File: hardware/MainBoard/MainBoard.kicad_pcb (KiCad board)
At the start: 4 copper layers, 28.6 x 59.4 mm, 54 parts, among them J1 Conn_02x16_Top_Bottom, J2 Conn_02x16_Top_Bottom, J3 USB_C_Receptacle_USB2.0_16P, J4 En_A, J5 En_B, J6 Micro_SD_Card_Det2, J7 Conn_02x16_Top_Bottom, Q1 MMBT2222A, U1 ESP32-S3-WROOM-1, U2 AMS1117-3.3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

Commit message: main board stuff
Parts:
- J1: moved to F.Cu
- J2: moved to B.Cu
- moved G*** 38.1 mm to (35.6, 70.9)
- moved J1 25.0 mm to (58.8, 91.8), turned to -90 degrees
- moved BOOT1 15.4 mm to (50.5, 64.7)
- moved R12 15.4 mm to (50.2, 68.6)
- moved J4 15.4 mm to (50.3, 71.0)
- moved J5 15.4 mm to (50.3, 74.6)
- moved R10 15.4 mm to (50.1, 61.0)
- moved C14 15.4 mm to (49.6, 59.8)
- moved C16 15.4 mm to (49.9, 72.8)
- moved J2 13.9 mm to (66.4, 69.8), turned to 90 degrees
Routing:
- net CONN_VCC: track 28.9 -> 0.00 mm, vias 7 -> 0
- net CHIP_PU: track 28.8 -> 0.00 mm, vias 1 -> 0
- net CONN_GND: track 16.0 -> 0.00 mm, vias 14 -> 0
- net GPIO0: track 15.4 -> 0.00 mm, vias 1 -> 0
- net CONN_3V: track 11.5 -> 0.00 mm
- net SD_DET: track 10.9 -> 0.00 mm, vias 2 -> 0
- net Net-(D2-A): track 1.98 -> 0.00 mm, vias 1 -> 0
- net Net-(D1-A): track 1.97 -> 0.00 mm, vias 1 -> 0
- net CONN_15: track 1.70 -> 0.00 mm, vias 1 -> 0
- net CONN_14: track 1.70 -> 0.00 mm, vias 1 -> 0
- net CONN_3: track 0.61 -> 0.00 mm, vias 1 -> 0
- net unconnected-(U1-TXD0-Pad37): vias 1 -> 0
- net unconnected-(U1-RXD0-Pad36): vias 1 -> 0
- net unconnected-(U1-IO9-Pad17): vias 1 -> 0
- net unconnected-(U1-IO8-Pad12): vias 1 -> 0
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
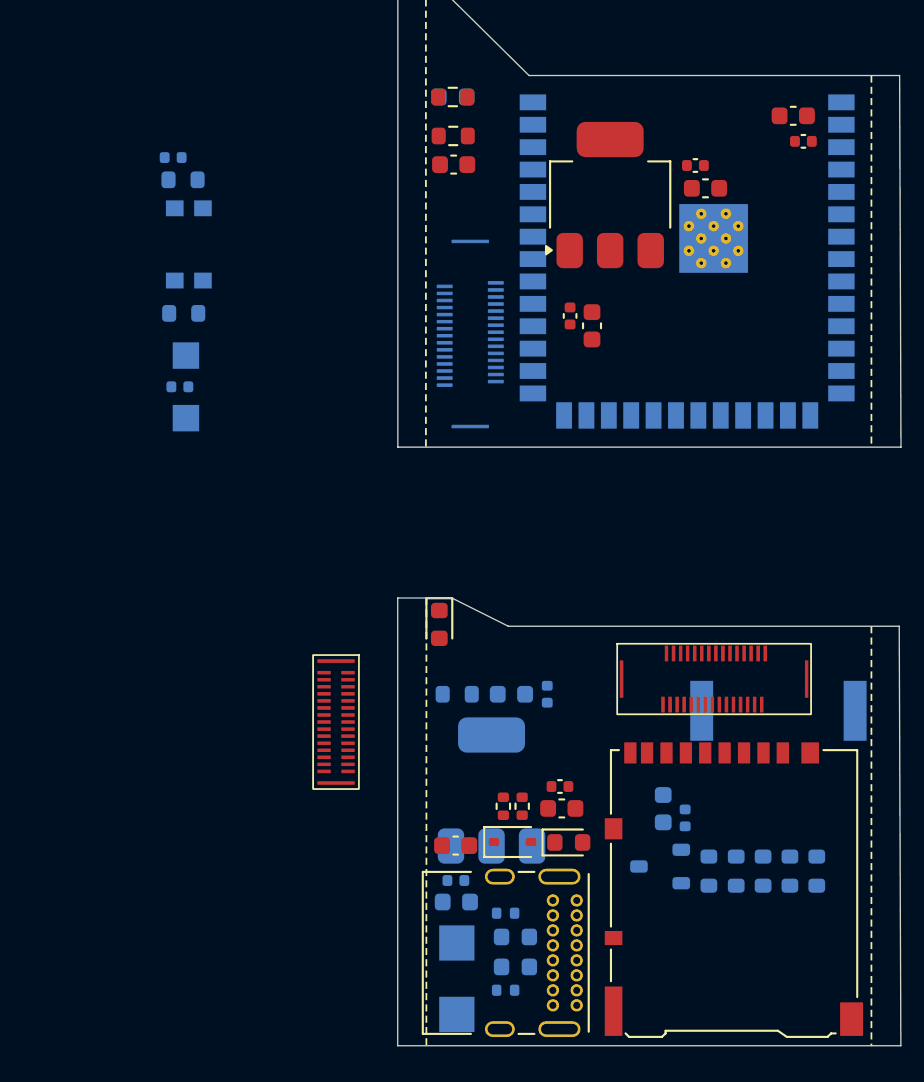
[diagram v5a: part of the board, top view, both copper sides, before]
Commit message: start arranging componnets for rack layout
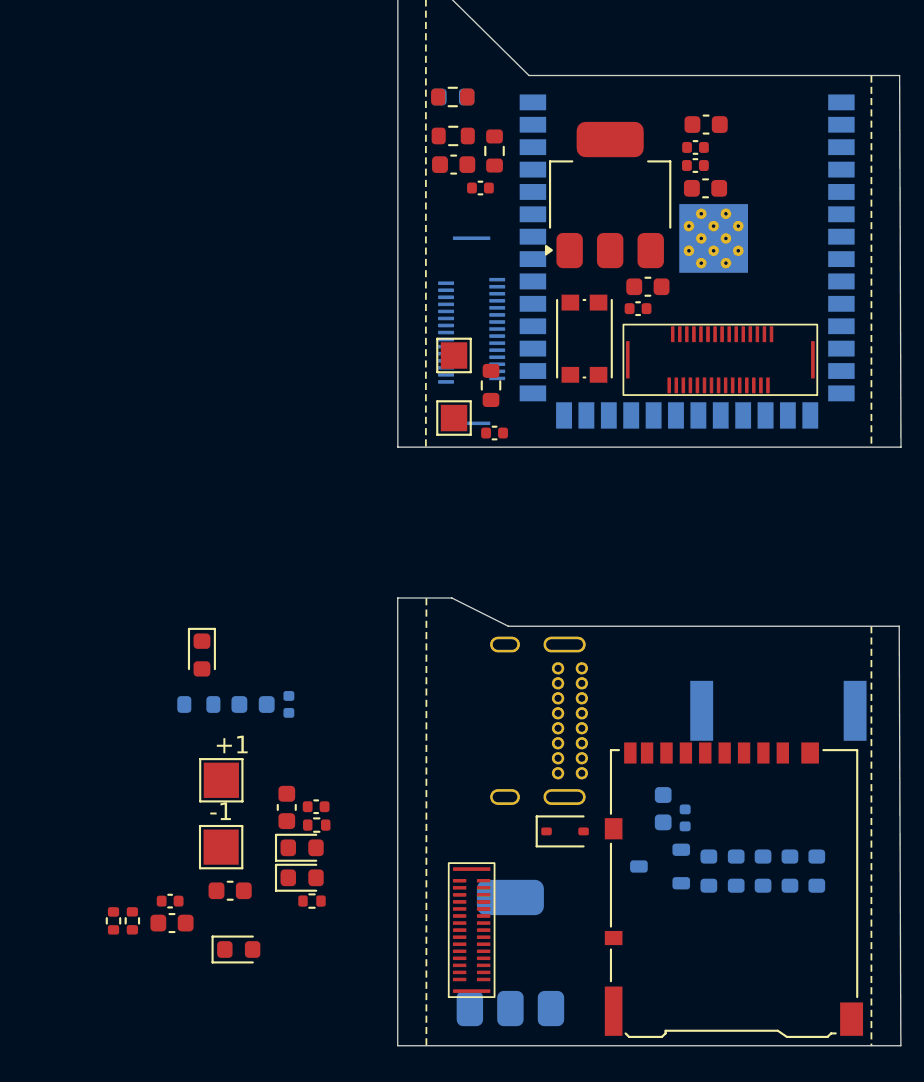
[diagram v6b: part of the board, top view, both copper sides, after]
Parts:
- +1, -1, BOOT1, C14, C16, C8, C9, D5, D6, J4, J5, R10, R12, R4, R5: moved to F.Cu
- J3: moved to B.Cu
- moved BOOT1 23.1 mm to (72.9, 70.0)
- moved C13 23.1 mm to (49.4, 102.0)
- moved R1 23.1 mm to (47.3, 103.1)
- moved C12 23.1 mm to (49.5, 103.2)
- moved R2 23.1 mm to (46.2, 103.1)
- moved D3 19.7 mm to (53.3, 104.7)
- moved J7 18.1 mm to (80.6, 71.2), turned to 180 degrees
- moved C16 18.0 mm to (67.8, 75.4), turned to 180 degrees
- moved R12 17.9 mm to (67.6, 72.7), turned to 90 degrees
- moved R10 17.7 mm to (67.8, 59.4), turned to -90 degrees
- moved C14 17.5 mm to (67.0, 61.5), turned to 180 degrees
- moved -1 16.4 mm to (52.3, 98.9), turned to 0 degrees
- moved +1 16.2 mm to (52.3, 95.1), turned to 0 degrees
- moved J4 15.2 mm to (65.5, 71.0), turned to 0 degrees
- moved J5 15.2 mm to (65.5, 74.5), turned to 0 degrees
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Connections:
- D5 pad 1: CONN_14 -> CONN_22
- D6 pad 1: CONN_15 -> CONN_23
- J1 pad 30: RET -> CONN_21
- J2 pad 15: RET -> CONN_29
- J2 pad 30: CONN_14 -> CONN_21
- J3 pad A6: CONN_15 -> CONN_23
- J3 pad A7: CONN_14 -> CONN_22
- J3 pad B6: CONN_15 -> CONN_23
- J3 pad B7: CONN_14 -> CONN_22
- J6 pad 1: CONN_23 -> CONN_24
- J6 pad 2: CONN_24 -> CONN_25
- J6 pad 3: CONN_25 -> CONN_26
- J6 pad 5: CONN_26 -> CONN_27
- J6 pad 7: CONN_27 -> CONN_28
- J6 pad 8: CONN_28 -> CONN_29
- J7 pad 1: unconnected-(J7-Pin_1-Pad1) -> CONN_0
- J7 pad 10: unconnected-(J7-Pin_10-Pad10) -> CONN_9
- J7 pad 11: unconnected-(J7-Pin_11-Pad11) -> CONN_10
- J7 pad 12: unconnected-(J7-Pin_12-Pad12) -> CONN_11
- J7 pad 13: unconnected-(J7-Pin_13-Pad13) -> CONN_12
- J7 pad 14: unconnected-(J7-Pin_14-Pad14) -> CONN_13
- J7 pad 15: unconnected-(J7-Pin_15-Pad15) -> CONN_14
- J7 pad 16: unconnected-(J7-Pin_16-Pad16) -> CONN_15
- J7 pad 2: unconnected-(J7-Pin_2-Pad2) -> CONN_1
- J7 pad 3: unconnected-(J7-Pin_3-Pad3) -> CONN_2
- J7 pad 4: unconnected-(J7-Pin_4-Pad4) -> CONN_3
- J7 pad 5: unconnected-(J7-Pin_5-Pad5) -> CONN_4
- J7 pad 6: unconnected-(J7-Pin_6-Pad6) -> CONN_5
- J7 pad 7: unconnected-(J7-Pin_7-Pad7) -> CONN_6
- J7 pad 8: unconnected-(J7-Pin_8-Pad8) -> CONN_7
- J7 pad 9: unconnected-(J7-Pin_9-Pad9) -> CONN_8
- Q1 pad 1: CONN_12 -> HATS_ENABLE
- R11 pad 2: CONN_23 -> CONN_24
- R6 pad 2: CONN_25 -> CONN_26
- R7 pad 2: CONN_27 -> CONN_28
- R8 pad 2: CONN_24 -> CONN_25
- R9 pad 2: CONN_28 -> CONN_29
- U1 pad 13: CONN_14 -> CONN_22
- U1 pad 14: CONN_15 -> CONN_23
- U1 pad 20: CONN_12 -> HATS_ENABLE
- U1 pad 21: RET -> CONN_21
- U1 pad 28: CONN_23 -> CONN_24
- U1 pad 29: CONN_24 -> CONN_25
- U1 pad 30: CONN_25 -> CONN_26
- U1 pad 32: CONN_26 -> CONN_27
- U1 pad 33: CONN_27 -> CONN_28
- U1 pad 34: CONN_28 -> CONN_29
- U1 pad 38: CONN_4 -> unconnected-(U1-IO2-Pad38)
- U1 pad 39: CONN_3 -> unconnected-(U1-IO1-Pad39)

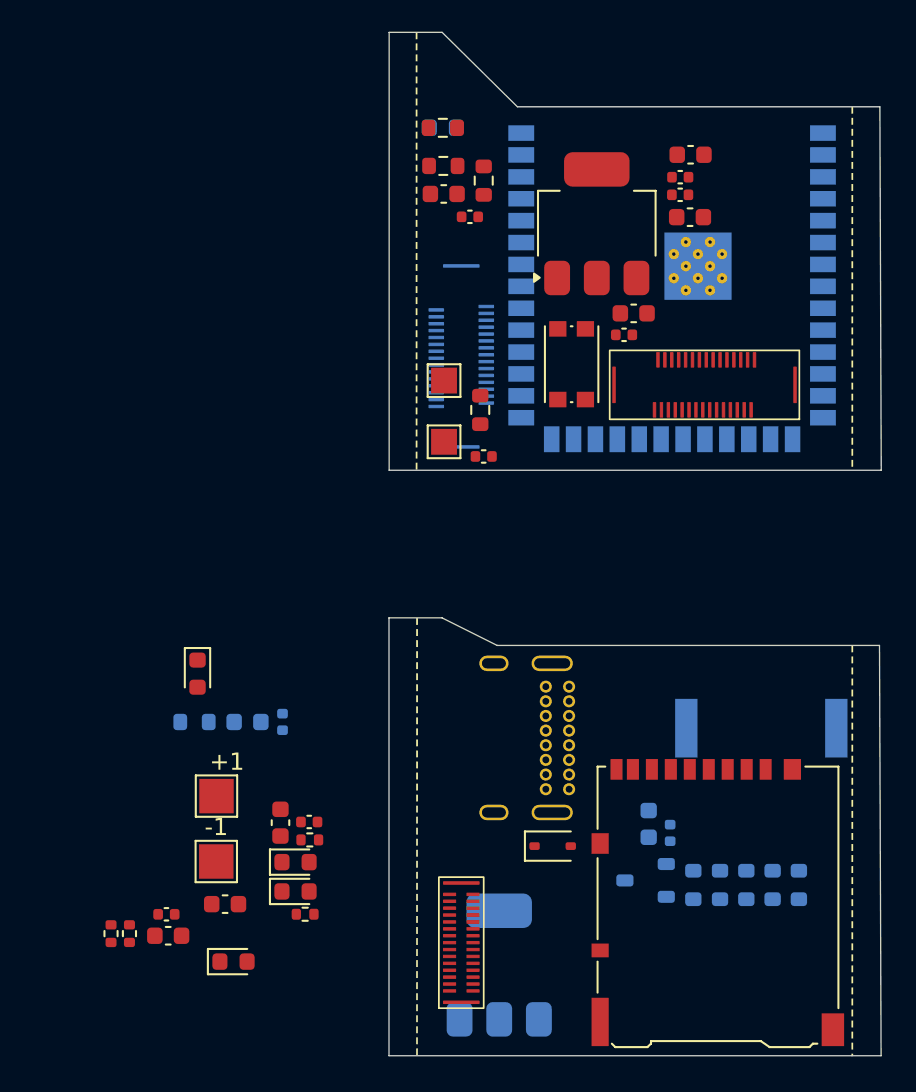
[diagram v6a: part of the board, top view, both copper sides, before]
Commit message: started final traces
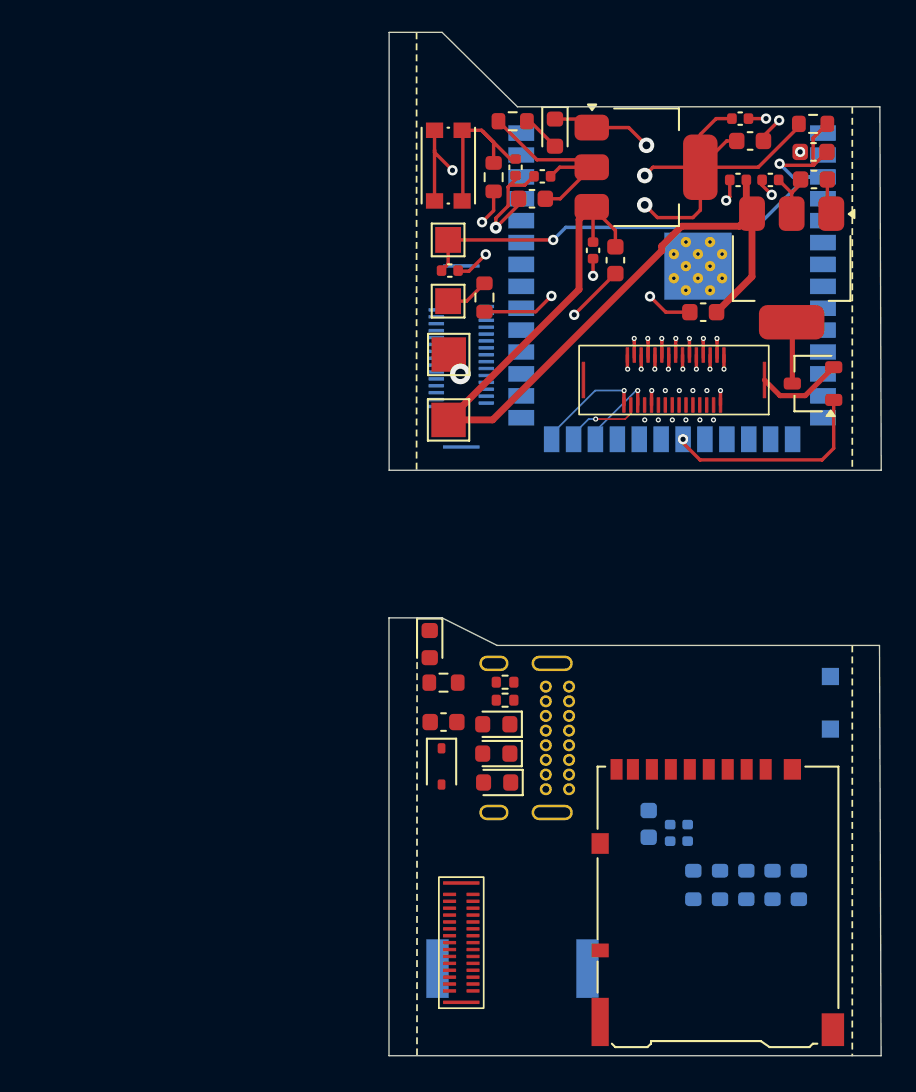
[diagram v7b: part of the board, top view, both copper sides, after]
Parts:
- removed the C12 at (49.5, 103.2)
- removed the R1 at (47.3, 103.1)
- removed the R2 at (46.2, 103.1)
- added I2C_CLK1: Conn_01x01, TestPoint:TestPoint_Pad_1.0x1.0mm, B.Cu at (87.9, 88.2)
- added I2C_DAT1: Conn_01x01, TestPoint:TestPoint_Pad_1.0x1.0mm, B.Cu at (87.9, 91.2)
- C10, C11, D1, Q1, R3, U3: moved to F.Cu
- C13: moved to B.Cu
- moved C10 45.5 mm to (87.0, 59.3), turned to 0 degrees
- moved C9 44.8 mm to (82.6, 59.4)
- moved U3 43.8 mm to (85.7, 64.5), turned to -90 degrees
- moved C11 42.3 mm to (84.4, 59.4), turned to 180 degrees
- moved C8 38.4 mm to (80.5, 67.0), turned to 180 degrees
- moved -1 32.4 mm to (65.8, 69.5), turned to 180 degrees
- moved C13 30.6 mm to (79.6, 97.2), turned to -90 degrees
- moved Q1 30.4 mm to (86.9, 71.2)
- moved +1 25.6 mm to (65.8, 73.3), turned to 180 degrees
- moved R1 21.6 mm to (86.9, 56.1)
- moved C1 21.6 mm to (86.9, 57.7)
- moved BZ1 20.1 mm to (69.5, 105.1)
- moved D3 18.5 mm to (68.6, 94.3), turned to 180 degrees
- moved R4 17.0 mm to (69.0, 89.5), turned to 180 degrees
- moved C12 16.5 mm to (65.5, 90.8), turned to 0 degrees
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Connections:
- J1 pad 30: CONN_21 -> CONN_29
- J2 pad 1: CONN_16 -> CONN_15
- J2 pad 2: CONN_15 -> CONN_16
- J2 pad 30: CONN_21 -> CONN_14
- J7 pad 1: CONN_0 -> DATA0
- J7 pad 10: CONN_9 -> DATA9
- J7 pad 11: CONN_10 -> DATA10
- J7 pad 12: CONN_11 -> DATA11
- J7 pad 13: CONN_12 -> DATA12
- J7 pad 14: CONN_13 -> DATA13
- J7 pad 15: CONN_14 -> DATA14
- J7 pad 16: CONN_15 -> DATA15
- J7 pad 2: CONN_1 -> DATA1
- J7 pad 25: unconnected-(J7-Pin_25-Pad25) -> RET
- J7 pad 26: unconnected-(J7-Pin_26-Pad26) -> INDEX4
- J7 pad 27: unconnected-(J7-Pin_27-Pad27) -> INDEX3
- J7 pad 28: unconnected-(J7-Pin_28-Pad28) -> INDEX2
- J7 pad 29: unconnected-(J7-Pin_29-Pad29) -> INDEX1
- J7 pad 3: CONN_2 -> DATA2
- J7 pad 30: unconnected-(J7-Pin_30-Pad30) -> INDEX0
- J7 pad 31: unconnected-(J7-Pin_31-Pad31) -> CONN_5V
- J7 pad 32: unconnected-(J7-Pin_32-Pad32) -> CONN_GND
- J7 pad 4: CONN_3 -> DATA3
- J7 pad 5: CONN_4 -> DATA4
- J7 pad 6: CONN_5 -> DATA5
- J7 pad 7: CONN_6 -> DATA6
- J7 pad 8: CONN_7 -> DATA7
- J7 pad 9: CONN_8 -> DATA8
- U1 pad 10: unconnected-(U1-IO17-Pad10) -> DATA11
- U1 pad 11: unconnected-(U1-IO18-Pad11) -> DATA12
- U1 pad 12: unconnected-(U1-IO8-Pad12) -> DATA13
- U1 pad 15: unconnected-(U1-IO3-Pad15) -> DATA14
- U1 pad 16: unconnected-(U1-IO46-Pad16) -> DATA15
- U1 pad 17: unconnected-(U1-IO9-Pad17) -> CONN_15
- U1 pad 19: unconnected-(U1-IO11-Pad19) -> CONN_14
- U1 pad 21: CONN_21 -> RET
- U1 pad 22: unconnected-(U1-IO14-Pad22) -> INDEX4
- U1 pad 23: unconnected-(U1-IO21-Pad23) -> INDEX3
- U1 pad 24: unconnected-(U1-IO47-Pad24) -> INDEX2
- U1 pad 25: unconnected-(U1-IO48-Pad25) -> INDEX1
- U1 pad 26: unconnected-(U1-IO45-Pad26) -> INDEX0
- U1 pad 35: unconnected-(U1-IO42-Pad35) -> DATA7
- U1 pad 36: unconnected-(U1-RXD0-Pad36) -> DATA6
- U1 pad 37: unconnected-(U1-TXD0-Pad37) -> DATA5
- U1 pad 38: unconnected-(U1-IO2-Pad38) -> DATA4
- U1 pad 39: unconnected-(U1-IO1-Pad39) -> DATA3
- U1 pad 4: unconnected-(U1-IO4-Pad4) -> DATA0
- U1 pad 5: unconnected-(U1-IO5-Pad5) -> DATA1
- U1 pad 6: unconnected-(U1-IO6-Pad6) -> DATA2
- U1 pad 7: unconnected-(U1-IO7-Pad7) -> DATA8
- U1 pad 8: unconnected-(U1-IO15-Pad8) -> DATA9
- U1 pad 9: unconnected-(U1-IO16-Pad9) -> DATA10
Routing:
- net CONN_3V: track 0.00 -> 52.3 mm
- net CONN_VCC: track 0.00 -> 42.3 mm, vias 0 -> 4
- net CONN_GND: track 0.00 -> 36.6 mm, vias 0 -> 13
- net CHIP_PU: track 0.00 -> 33.9 mm, vias 0 -> 2
- net HATS_ENABLE: track 0.00 -> 12.4 mm, vias 0 -> 1
- net GPIO0: track 0.00 -> 9.99 mm
- net VCC_5V: track 0.00 -> 6.84 mm
- net INDEX0: track 0.00 -> 6.39 mm, vias 0 -> 1
- net CONN_5V: track 0.00 -> 5.08 mm
- net INDEX2: track 0.00 -> 4.74 mm, vias 0 -> 1
- net INDEX1: track 0.00 -> 4.61 mm, vias 0 -> 1
- net Net-(J4-Pin_1): track 0.00 -> 2.54 mm
- net Net-(D1-A): track 0.00 -> 2.23 mm
- net DATA11: track 0.00 -> 0.97 mm, vias 0 -> 1
- net DATA3: track 0.00 -> 0.96 mm, vias 0 -> 1
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
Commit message: finished 1x1 main board
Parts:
- removed the C13 at (79.6, 97.2)
- added G***: LOGO, lib:tacos_logo, B.Cu at (77.8, 86.2)
- +1: value LIPO GND -> LIPO PWR
- -1: value LIPO PWR -> LIPO GND
- C13, C15, R11, R6, R7, R8, R9: moved to F.Cu
- moved G*** 42.1 mm to (75.1, 56.6)
- moved R7 11.8 mm to (77.7, 89.1)
- moved R9 11.8 mm to (76.2, 89.1)
- moved R6 11.2 mm to (82.7, 89.1)
- moved R8 11.2 mm to (84.2, 89.1)
- moved R11 11.2 mm to (85.8, 89.1)
- moved R5 9.06 mm to (69.1, 97.5)
- moved C15 9.04 mm to (80.9, 88.5), turned to 90 degrees
- moved C13 7.97 mm to (79.6, 89.1), turned to 90 degrees
- moved C8 0.51 mm to (80.0, 67.0)
- renumbered U1 to ESP32-S3-WROOM-1
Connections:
- net CONN_3V renamed LIPO PWR
- C10 pad 1: VCC_5V -> CONN_VCC
- C11 pad 1: VCC_5V -> CONN_VCC
- D5 pad 1: CONN_22 -> CONN_2
- D6 pad 1: CONN_23 -> CONN_0
- ESP32-S3-WROOM-1 pad 13: CONN_22 -> CONN_2
- ESP32-S3-WROOM-1 pad 14: CONN_23 -> CONN_0
- ESP32-S3-WROOM-1 pad 19: CONN_14 -> CONN_16
- ESP32-S3-WROOM-1 pad 28: CONN_24 -> CONN_6
- ESP32-S3-WROOM-1 pad 29: CONN_25 -> CONN_7
- ESP32-S3-WROOM-1 pad 30: CONN_26 -> CONN_10
- ESP32-S3-WROOM-1 pad 31: SD_DET -> CONN_11
- ESP32-S3-WROOM-1 pad 32: CONN_27 -> CONN_14
- I2C_DAT1 pad 1: CONN_14 -> CONN_16
- J1 pad 18: CONN_17 -> BZR
- J2 pad 3: CONN_17 -> BZR
- J3 pad A6: CONN_23 -> CONN_0
- J3 pad A7: CONN_22 -> CONN_2
- J3 pad B6: CONN_23 -> CONN_0
- J3 pad B7: CONN_22 -> CONN_2
- J6 pad 1: CONN_24 -> CONN_6
- J6 pad 10: SD_DET -> CONN_11
- J6 pad 2: CONN_25 -> CONN_7
- J6 pad 3: CONN_26 -> CONN_10
- J6 pad 5: CONN_27 -> CONN_14
- J6 pad 9: SD_DET -> CONN_11
- J7 pad 1: DATA0 -> DATA9
- J7 pad 10: DATA9 -> DATA5
- J7 pad 11: DATA10 -> DATA4
- J7 pad 12: DATA11 -> DATA3
- J7 pad 13: DATA12 -> DATA2
- J7 pad 14: DATA13 -> DATA1
- J7 pad 15: DATA14 -> DATA0
- J7 pad 16: DATA15 -> DATA14
- J7 pad 17: unconnected-(J7-Pin_17-Pad17) -> DATA15
- J7 pad 2: DATA1 -> DATA10
- J7 pad 26: INDEX4 -> INDEX0
- J7 pad 27: INDEX3 -> INDEX1
- J7 pad 29: INDEX1 -> INDEX3
- J7 pad 3: DATA2 -> DATA11
- J7 pad 30: INDEX0 -> INDEX4
- J7 pad 4: DATA3 -> DATA12
- J7 pad 5: DATA4 -> DATA13
- J7 pad 6: DATA5 -> unconnected-(J7-Pin_6-Pad6)
- J7 pad 7: DATA6 -> DATA8
- J7 pad 9: DATA8 -> DATA6
- Q1 pad 3: VCC_5V -> CONN_VCC
- R11 pad 2: CONN_24 -> CONN_6
- R3 pad 1: VCC_5V -> CONN_VCC
- R6 pad 2: CONN_26 -> CONN_10
- R8 pad 2: CONN_25 -> CONN_7
- U3 pad 2: VCC_5V -> CONN_VCC
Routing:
- net CONN_VCC: track 42.3 -> 103.0 mm, vias 4 -> 15
- net CONN_15: track 0.00 -> 60.4 mm, vias 0 -> 1
- net CONN_16: track 0.00 -> 54.4 mm, vias 0 -> 1
- net CONN_GND: track 36.6 -> 88.8 mm, vias 13 -> 30
- net CONN_2: track 0.00 -> 45.8 mm, vias 0 -> 3
- net CONN_0: track 0.00 -> 45.7 mm, vias 0 -> 2
- net BZR: track 0.00 -> 36.8 mm, vias 0 -> 2
- net CONN_6: track 0.00 -> 30.8 mm, vias 0 -> 2
- net CONN_28: track 0.00 -> 28.3 mm, vias 0 -> 2
- net CONN_7: track 0.00 -> 28.0 mm, vias 0 -> 2
- net CONN_29: track 0.00 -> 27.3 mm, vias 0 -> 2
- net CONN_10: track 0.00 -> 26.5 mm, vias 0 -> 2
- net CONN_11: track 0.00 -> 24.4 mm, vias 0 -> 3
- net CONN_14: track 0.00 -> 19.1 mm, vias 0 -> 2
- net DATA0: track 0.82 -> 17.2 mm
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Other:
- board size 28.6 x 59.4 mm -> 28 x 58.4 mm
- board text added: "+"
- board text added: "-"
- board text added: "Enable"
- board text added: "Power"
- board text added: "T.A.C.O.S. Main Board"
